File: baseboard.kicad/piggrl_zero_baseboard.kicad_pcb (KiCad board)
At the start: 2 copper layers, 101 x 43.9 mm, 58 parts, among them P1 PowerBoost 500c, P2 I2C, P3 USB_A, P4 Serial, Q1 IRF7309IPBF, Q3 Q_PMOS_DGS, Q4 MMBT2222, SW1 SW_PUSH, U1 gpio-header_zero, U2 2.2_tft_ili9340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

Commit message: added connection from low-bat on the powerboost to the (till now) unused ID_SD pin
since we already used ID_SC for display-pwm, the whole board won't turn into an spec-compliant hat anyway...
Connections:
- U1 pad 27: Net-(U1-Pad27) -> /LowBatOut
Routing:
- net /LowBatOut: track 0.00 -> 33.2 mm, vias 0 -> 2

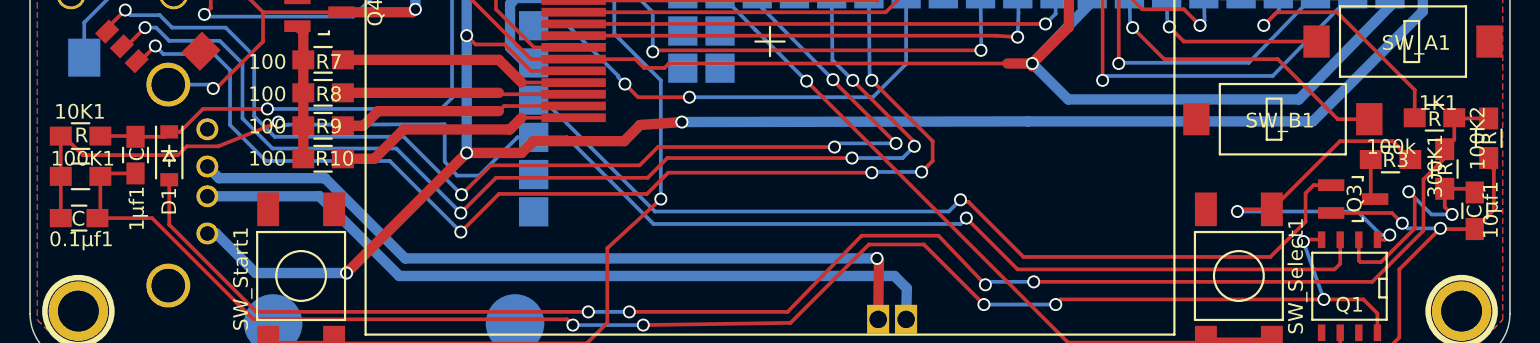
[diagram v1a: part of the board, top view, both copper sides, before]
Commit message: fixed switched Value/Reference in soft_power schematic (showed in bad BOM references)
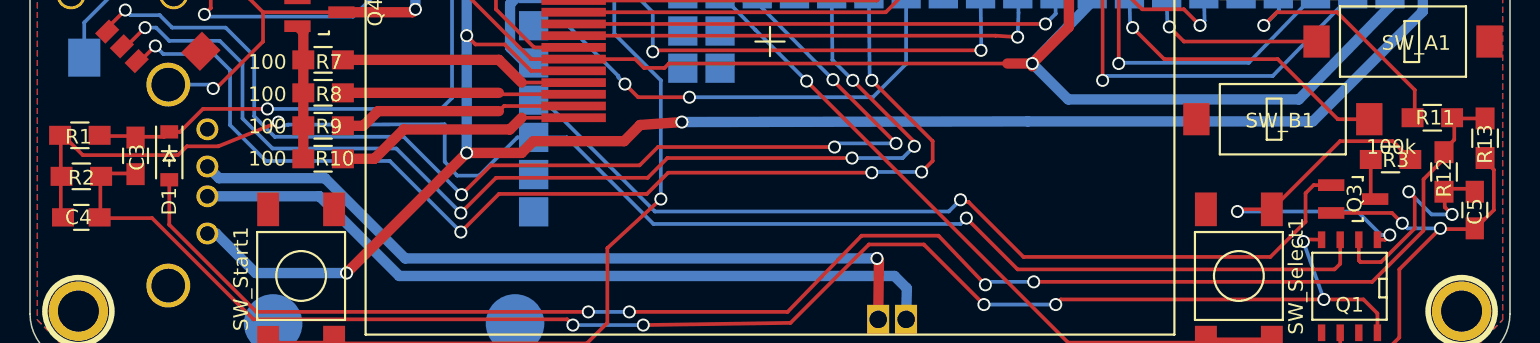
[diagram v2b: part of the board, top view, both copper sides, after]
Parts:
- removed 0.1µf1, 10µf1, 1µf1: C, Capacitors_SMD:C_0805_HandSoldering
- removed 100K1, 100K2, 10K1, 1K1, 300K1: R, Resistors_SMD:R_0805_HandSoldering
- added C3: 1µF, Capacitors_SMD:C_0805_HandSoldering, F.Cu at (124.2, 138.8)
- added C4: 0.1µF, Capacitors_SMD:C_0805_HandSoldering, F.Cu at (120.5, 143.0)
- added C5: 10µF, Capacitors_SMD:C_0805_HandSoldering, F.Cu at (215.6, 142.5)
- added R1: 10k, Resistors_SMD:R_0805_HandSoldering, F.Cu at (120.4, 137.4)
- added R11: 1.1k, Resistors_SMD:R_0805_HandSoldering, F.Cu at (212.7, 136.2)
- added R12: 300k, Resistors_SMD:R_0805_HandSoldering, F.Cu at (213.5, 139.9)
- added R13: 100k, Resistors_SMD:R_0805_HandSoldering, F.Cu at (216.3, 137.6)
- added R2: 100k, Resistors_SMD:R_0805_HandSoldering, F.Cu at (120.5, 140.2)

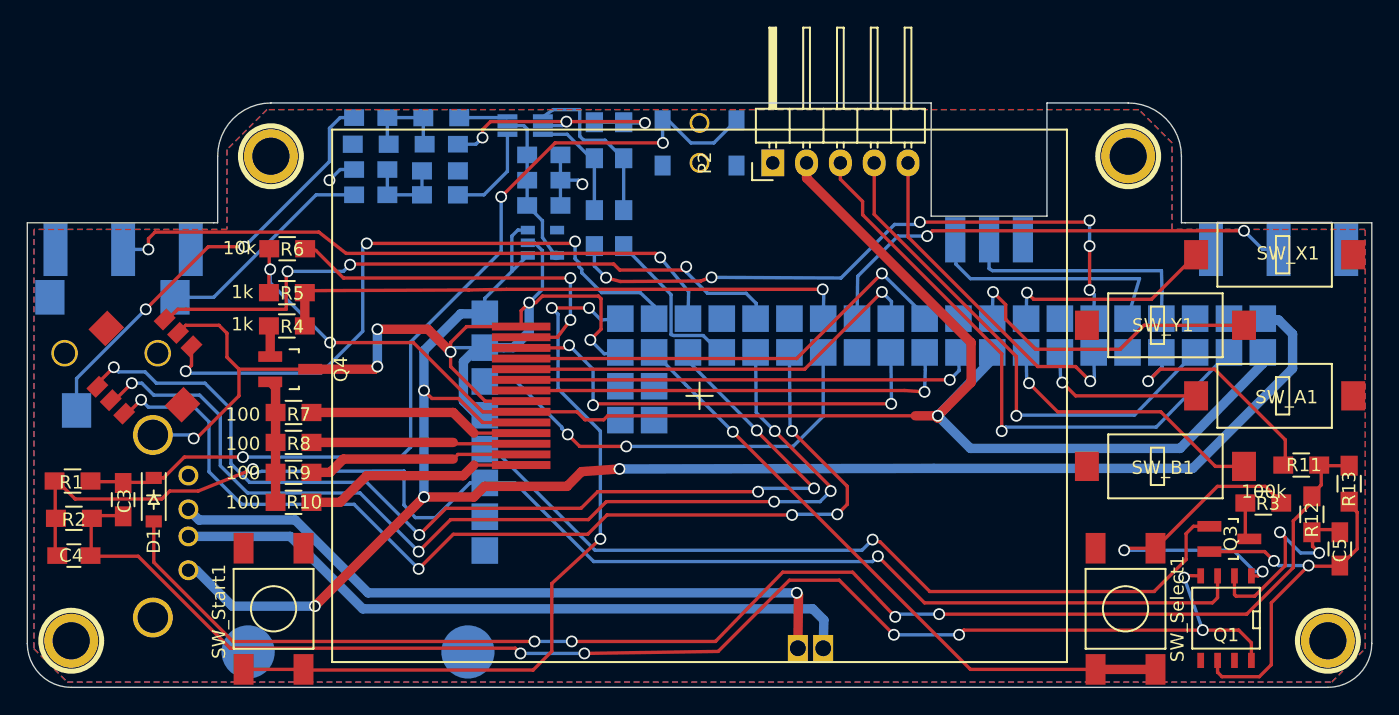
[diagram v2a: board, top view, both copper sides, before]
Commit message: cleanup of silkscreen for better readability during assembly
generated and pushed new boardfiles to oshpark
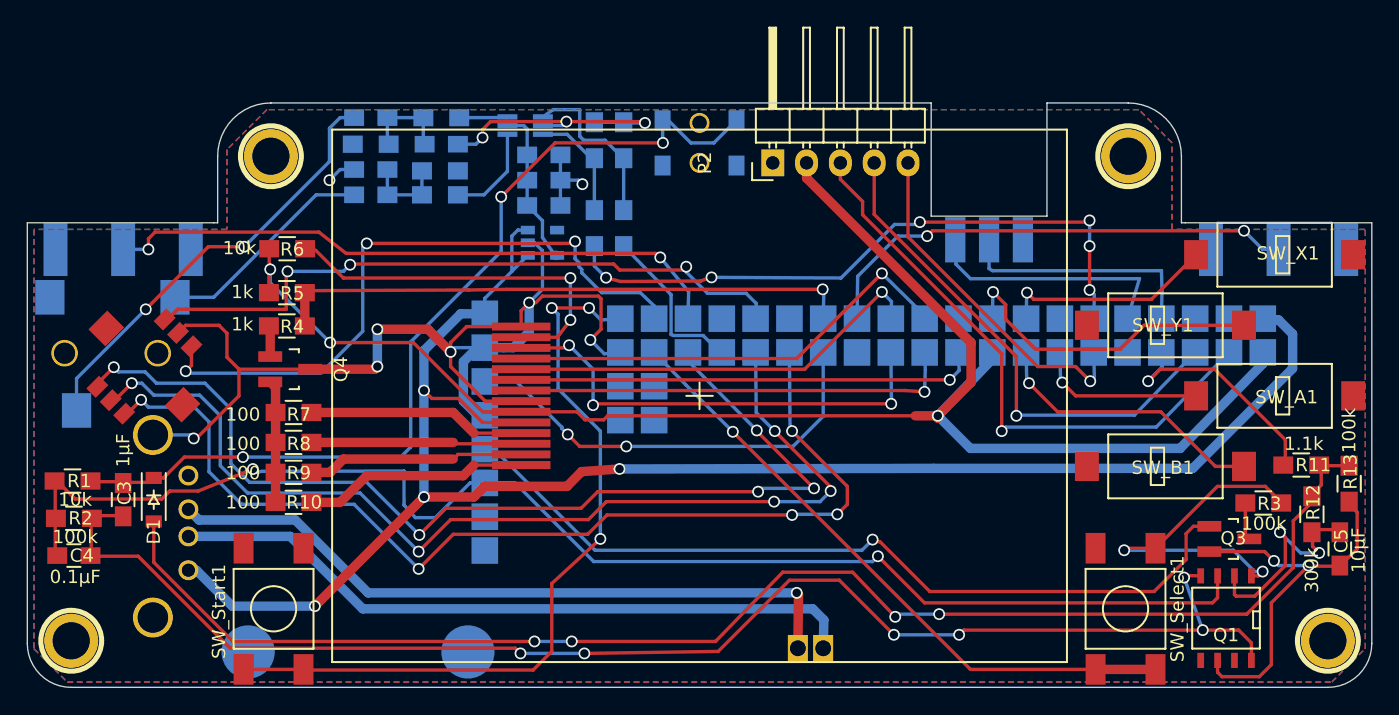
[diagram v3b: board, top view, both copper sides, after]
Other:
- board text added: "2016-03-05"
- board text removed: "2016-02-13"
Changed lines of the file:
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@@
     (links 139)
     (no_connects 9)
-    (area 116.949999 108.949999 218.050001 152.950001)
+    (area 113.016999 90.926522 234 163.200001)
     (thickness 1.6)
     (drawings 28)
@@
     (31 B.Cu signal)
     (32 B.Adhes user)
-    (33 F.Adhes user)
+    (33 F.Adhes user hide)
     (34 B.Paste user)
-    (35 F.Paste user)
+    (35 F.Paste user hide)
     (36 B.SilkS user)
-    (37 F.SilkS user)
+    (37 F.SilkS user hide)
     (38 B.Mask user)
-    (39 F.Mask user)
+    (39 F.Mask user hide)
     (40 Dwgs.User user)
     (41 Cmts.User user)
@@
     (aux_axis_origin 0 0)
     (grid_origin 12 12)
-    (visible_elements FFFFFFFF)
+    (visible_elements FFFFFF7F)
     (pcbplotparams
       (layerselection 0x010f0_80000001)
@@
     (tags DEV)
     (path 1pin)
-    (fp_text reference 1PIN (at -0.05 -1.7) (layer F.SilkS) hide
+    (fp_text reference 1PIN (at -0.1 0) (layer F.SilkS) hide
       (effects (font (size 1.016 1.016) (thickness 0.254)))
     )
@@
       (effects (font (size 1 1) (thickness 0.15)) (justify mirror))
     )
-    (fp_text value 10u (at -0.05 -1.39) (layer B.Fab)
+    (fp_text value 10u (at 0.5 -8.1) (layer B.SilkS)
       (effects (font (size 1 1) (thickness 0.15)) (justify mirror))
     )
@@
       (effects (font (size 1 1) (thickness 0.15)) (justify mirror))
     )
-    (fp_text value 10n (at 0.05 -1.44) (layer B.Fab)
+    (fp_text value 10n (at 0.4 -7.7) (layer B.SilkS)
       (effects (font (size 1 1) (thickness 0.15)) (justify mirror))
     )
@@
       (effects (font (size 1 1) (thickness 0.15)) (justify mirror))
     )
-    (fp_text value 100n (at 0 -2.1 180) (layer B.Fab)
+    (fp_text value 100n (at -0.4 8.6 180) (layer B.SilkS)
       (effects (font (size 1 1) (thickness 0.15)) (justify mirror))
     )
@@
     (tags SOD-123)
     (attr smd)
-    (fp_text reference D1 (at 3.1 0 270) (layer F.SilkS)
+    (fp_text reference D1 (at 2.4 0 450) (layer F.SilkS)
       (effects (font (size 1 1) (thickness 0.15)))
     )
@@
       (effects (font (size 1 1) (thickness 0.15)))
     )
-    (fp_text value I2C (at 0 -3.1 90) (layer F.Fab)
+    (fp_text value I2C (at 2.5 0 90) (layer F.Fab)
       (effects (font (size 1 1) (thickness 0.15)))
     )
@@
     (tags SOT-23)
     (attr smd)
-    (fp_text reference Q3 (at -0.05 -0.1 270) (layer F.SilkS)
+    (fp_text reference Q3 (at -0.05 -0.3 360) (layer F.SilkS)
       (effects (font (size 1 1) (thickness 0.15)))
     )
@@
     (tags "resistor 0805")
     (attr smd)
-    (fp_text reference R3 (at 0.35 0.05) (layer F.SilkS)
+    (fp_text reference R3 (at 0.45 0.05) (layer F.SilkS)
       (effects (font (size 1 1) (thickness 0.15)))
     )
-    (fp_text value 100k (at 0.05 -0.85) (layer F.SilkS)
+    (fp_text value 100k (at 0.05 1.55) (layer F.SilkS)
       (effects (font (size 1 1) (thickness 0.15)))
     )
@@
       (effects (font (size 1 1) (thickness 0.15)) (justify mirror))
     )
-    (fp_text value 100 (at 3.6 0.1) (layer B.Fab)
+    (fp_text value 100 (at 3.6 0.1) (layer B.SilkS)
       (effects (font (size 1 1) (thickness 0.15)) (justify mirror))
     )
@@
       (effects (font (size 1 1) (thickness 0.15)) (justify mirror))
     )
-    (fp_text value 100 (at 0 -2.1 270) (layer B.Fab)
+    (fp_text value 100 (at 3.8 0.1 270) (layer B.SilkS)
       (effects (font (size 1 1) (thickness 0.15)) (justify mirror))
     )
@@
       (effects (font (size 1 1) (thickness 0.15)) (justify mirror))
     )
-    (fp_text value 470 (at 0 -2.1 90) (layer B.Fab)
+    (fp_text value 470 (at 4.3 0.3 90) (layer B.SilkS)
       (effects (font (size 1 1) (thickness 0.15)) (justify mirror))
     )
@@
       (effects (font (size 1 1) (thickness 0.15)) (justify mirror))
     )
-    (fp_text value 100 (at 0 -2.1 270) (layer B.Fab)
+    (fp_text value 100 (at 3.8 0 270) (layer B.SilkS)
       (effects (font (size 1 1) (thickness 0.15)) (justify mirror))
     )
@@
       (effects (font (size 1 1) (thickness 0.15)) (justify mirror))
     )
-    (fp_text value 470 (at 0 -2.54 90) (layer B.Fab)
+    (fp_text value 470 (at 4.4 0 90) (layer B.SilkS)
       (effects (font (size 1 1) (thickness 0.15)) (justify mirror))
     )
@@
       (effects (font (size 1 1) (thickness 0.15)) (justify mirror))
     )
-    (fp_text value NC7WZ16_Dual_Buffer (at -9.9 0 270) (layer B.Fab)
+    (fp_text value NC7WZ16_Dual_Buffer (at -10.8 1.2 270) (layer B.Fab)
       (effects (font (size 1 1) (thickness 0.15)) (justify mirror))
     )
@@
       (effects (font (size 1 1) (thickness 0.15)) (justify mirror))
     )
-    (fp_text value SW_PUSH (at 0.5 1.25 90) (layer B.Fab)
+    (fp_text value SW_PUSH (at 8.1 0.1 90) (layer B.Fab)
       (effects (font (size 1 1) (thickness 0.15)) (justify mirror))
     )
@@
     (tags "capacitor 0805")
     (attr smd)
-    (fp_text reference C3 (at -0.1 0.1 90) (layer F.SilkS)
+    (fp_text reference C3 (at 0.5 0.1 270) (layer F.SilkS)
       (effects (font (size 1 1) (thickness 0.15)))
     )
-    (fp_text value 1µF (at -2.6 0.1 90) (layer F.Fab)
+    (fp_text value 1µF (at 3.7 0 270) (layer F.SilkS)
       (effects (font (size 1 1) (thickness 0.15)))
     )
@@
     (tags "capacitor 0805")
     (attr smd)
-    (fp_text reference C4 (at 0.2 0 180) (layer F.SilkS)
+    (fp_text reference C4 (at -0.6 0 180) (layer F.SilkS)
       (effects (font (size 1 1) (thickness 0.15)))
     )
-    (fp_text value 0.1µF (at 0.1 -1.5 180) (layer F.Fab)
+    (fp_text value 0.1µF (at -0.1 -1.6 180) (layer F.SilkS)
       (effects (font (size 1 1) (thickness 0.15)))
     )
@@
     (tags "capacitor 0805")
     (attr smd)
-    (fp_text reference C5 (at 0.1 0 270) (layer F.SilkS)
+    (fp_text reference C5 (at -0.6 -0.1 270) (layer F.SilkS)
       (effects (font (size 1 1) (thickness 0.15)))
     )
-    (fp_text value 10µF (at 2.2 1.9 270) (layer F.Fab)
+    (fp_text value 10µF (at 0.1 -1.4 270) (layer F.SilkS)
       (effects (font (size 1 1) (thickness 0.15)))
     )
@@
     (tags "resistor 0805")
     (attr smd)
-    (fp_text reference R1 (at 0.1 -0.1 180) (layer F.SilkS)
+    (fp_text reference R1 (at -0.5 0 180) (layer F.SilkS)
       (effects (font (size 1 1) (thickness 0.15)))
     )
-    (fp_text value 10k (at 3.9 0 180) (layer F.Fab)
+    (fp_text value 10k (at -0.2 -1.4 180) (layer F.SilkS)
       (effects (font (size 1 1) (thickness 0.15)))
     )
@@
     (tags "resistor 0805")
     (attr smd)
-    (fp_text reference R2 (at 0 -0.1 180) (layer F.SilkS)
+    (fp_text reference R2 (at -0.5 0 180) (layer F.SilkS)
       (effects (font (size 1 1) (thickness 0.15)))
     )
-    (fp_text value 100k (at 4.3 0 180) (layer F.Fab)
+    (fp_text value 100k (at -0.1 -1.4 180) (layer F.SilkS)
       (effects (font (size 1 1) (thickness 0.15)))
     )
@@
     (tags "resistor 0805")
     (attr smd)
-    (fp_text reference R11 (at 0.2 0) (layer F.SilkS)
+    (fp_text reference R11 (at 0.9 0) (layer F.SilkS)
       (effects (font (size 1 1) (thickness 0.15)))
     )
-    (fp_text value 1.1k (at 0.1 -1.4 180) (layer F.Fab)
+    (fp_text value 1.1k (at 0.2 -1.6) (layer F.SilkS)
       (effects (font (size 1 1) (thickness 0.15)))
     )
@@
     (tags "resistor 0805")
     (attr smd)
-    (fp_text reference R12 (at 0.4 0 270) (layer F.SilkS)
+    (fp_text reference R12 (at -0.9 -0.1 270) (layer F.SilkS)
       (effects (font (size 1 1) (thickness 0.15)))
     )
-    (fp_text value 300k (at -1 -1.3 270) (layer F.Fab)
+    (fp_text value 300k (at 4.2 0 270) (layer F.SilkS)
       (effects (font (size 1 1) (thickness 0.15)))
     )
@@
     (tags "resistor 0805")
     (attr smd)
-    (fp_text reference R13 (at 0.4 0 270) (layer F.SilkS)
+    (fp_text reference R13 (at -0.9 -0.1 270) (layer F.SilkS)
       (effects (font (size 1 1) (thickness 0.15)))
     )
-    (fp_text value 100k (at -3.9 0.1 270) (layer F.Fab)
+    (fp_text value 100k (at -4 0 270) (layer F.SilkS)
       (effects (font (size 1 1) (thickness 0.15)))
     )
@@
     )
   )
-  (gr_text 2016-02-13 (at 171.1 120.5) (layer B.SilkS)
+  (gr_text 2016-03-05 (at 171.1 120.5) (layer B.SilkS)
     (effects (font (size 1.5 1.5) (thickness 0.3)) (justify mirror))
   )

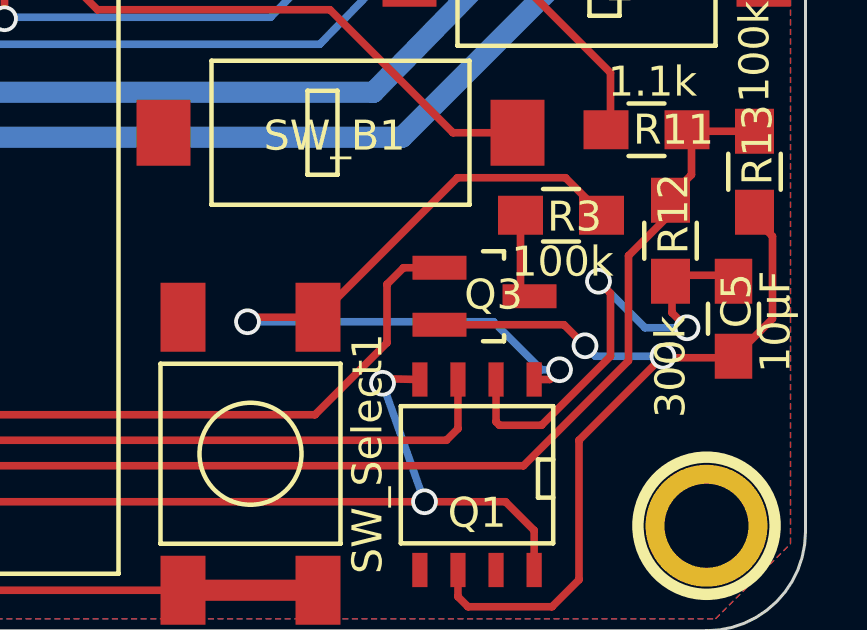
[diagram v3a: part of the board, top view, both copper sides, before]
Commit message: fixed wrong transistor pinout on softpower p-mosfet
common pinout is GSD and not DSG!
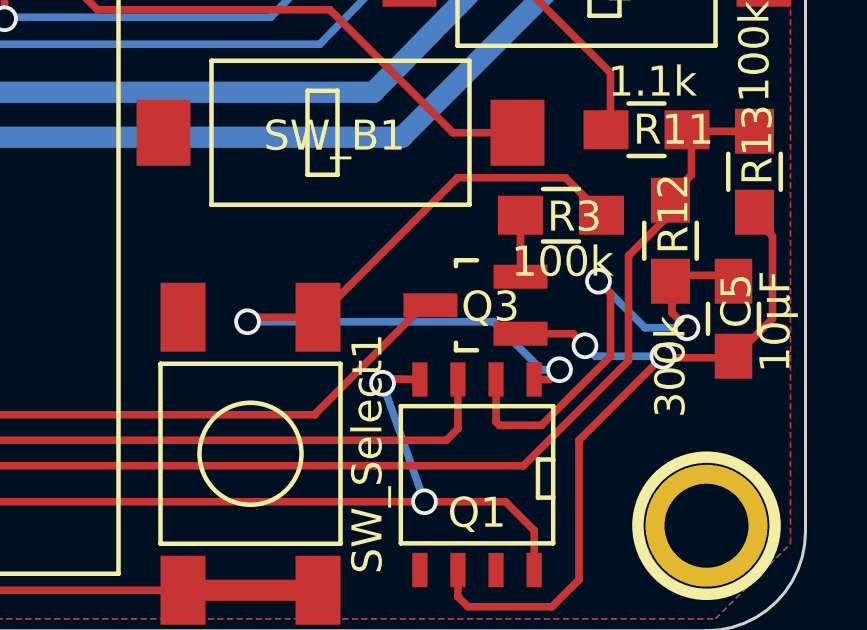
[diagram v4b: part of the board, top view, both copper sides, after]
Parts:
- Q3: value Q_PMOS_DGS -> Q_PMOS_GSD
- moved Q3 0.43 mm to (207.0, 142.1), turned to 90 degrees
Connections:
- Q3 pad 1: /Enable -> /soft_power_button/Vout
- Q3 pad 2: /soft_power_button/Vout -> Net-(Q3-Pad2)
- Q3 pad 3: Net-(Q3-Pad3) -> /Enable
- R3 pad 1: Net-(Q3-Pad3) -> Net-(Q3-Pad2)
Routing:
- net /soft_power_button/Vout: track 29.8 -> 27.0 mm
- net Net-(Q3-Pad3): track 2.82 -> 0.00 mm
- net Net-(Q3-Pad2): track 0.00 -> 2.05 mm
- net /Enable: track 62.7 -> 60.7 mm
